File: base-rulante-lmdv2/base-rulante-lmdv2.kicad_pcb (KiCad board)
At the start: 2 copper layers, 94 x 78.7 mm, 27 parts, among them J1 RJ_can, J2 RJ_can, J3 connector_power, J4 connector_power, J5 connector_power, U1 Nucleo_STM32G431KB, U2 LMD18200, U3 LMD18200, U4 MCP2551-I-SN

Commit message: carte IO
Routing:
- net GND: vias 0 -> 1
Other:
- board text added: "12V"
- board text added: "Joel Imbergamo 2023-AAA"
- board text added: "USB"
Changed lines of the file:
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@@
     (fp_rect (start 14.351 -0.889) (end 16.129 36.449)
       (stroke (width 0.12) (type solid)) (fill none) (layer "F.SilkS"))
-    (fp_arc (start 3.967155 -10.260847) (mid 4.012946 -10.18528) (end 4.029561 -10.0985)
-      (stroke (width 0.12) (type solid)) (layer "F.SilkS"))
-    (fp_arc (start 4.151131 -10.424759) (mid 4.243716 -10.27088) (end 4.275977 -10.094215)
-      (stroke (width 0.12) (type solid)) (layer "F.SilkS"))
-    (fp_arc (start 4.625988 -10.535212) (mid 4.709184 -10.688639) (end 4.875989 -10.74)
+    (fp_arc (start 3.967155 -10.260847) (mid 4.012928 -10.185275) (end 4.029561 -10.0985)
+      (stroke (width 0.12) (type solid)) (layer "F.SilkS"))
+    (fp_arc (start 4.151131 -10.424759) (mid 4.243692 -10.270872) (end 4.275977 -10.094215)
+      (stroke (width 0.12) (type solid)) (layer "F.SilkS"))
+    (fp_arc (start 4.625988 -10.535212) (mid 4.709181 -10.688645) (end 4.875989 -10.74)
       (stroke (width 0.12) (type solid)) (layer "F.SilkS"))
     (fp_arc (start 4.625989 -10.391818) (mid 4.709183 -10.545247) (end 4.875989 -10.596605)
@@
     (fp_arc (start 4.625989 -10.189999) (mid 4.597956 -10.120573) (end 4.529578 -10.090064)
       (stroke (width 0.12) (type solid)) (layer "F.SilkS"))
-    (fp_arc (start 10.575989 -10.739999) (mid 10.742844 -10.688681) (end 10.825988 -10.535211)
-      (stroke (width 0.12) (type solid)) (layer "F.SilkS"))
-    (fp_arc (start 10.575989 -10.596605) (mid 10.742846 -10.545287) (end 10.825988 -10.391817)
+    (fp_arc (start 10.575989 -10.739999) (mid 10.742816 -10.688675) (end 10.825988 -10.535211)
+      (stroke (width 0.12) (type solid)) (layer "F.SilkS"))
+    (fp_arc (start 10.575989 -10.596605) (mid 10.742818 -10.545281) (end 10.825988 -10.391817)
       (stroke (width 0.12) (type solid)) (layer "F.SilkS"))
     (fp_arc (start 10.922399 -10.090063) (mid 10.854026 -10.120573) (end 10.825988 -10.19)
@@
   (gr_line (start 167.64 149.86) (end 114.3 149.86)
     (stroke (width 0.1) (type default)) (layer "Edge.Cuts"))
+  (gr_text "Joel Imbergamo\n2023-AAA" (at 83.82 147.32) (layer "F.Cu")
+    (effects (font (size 1.5 1.5) (thickness 0.3) bold) (justify left bottom))
+  )
+  (gr_text "12V" (at 137.16 144.78) (layer "F.Cu")
+    (effects (font (size 1.5 1.5) (thickness 0.3) bold) (justify left bottom))
+  )
+  (gr_text "USB" (at 114.3 73.66) (layer "F.Cu")
+    (effects (font (size 1.5 1.5) (thickness 0.3) bold) (justify left bottom))
+  )
   (segment (start 116.84 132.08) (end 116.84 134.62) (width 0.5) (layer "F.Cu") (net 1))
   (segment (start 114.3 99.06) (end 121.675539 91.684461) (width 0.25) (layer "F.Cu") (net 1))
@@
   (segment (start 88.1525 81.28) (end 86.36 81.28) (width 1) (layer "B.Cu") (net 1))
   (segment (start 81.28 86.36) (end 81.28 106.68) (width 1) (layer "B.Cu") (net 1))
+  (via (at 139.7 134.62) (size 0.8) (drill 0.4) (layers "F.Cu" "B.Cu") (free) (net 2))
   (segment (start 158.4925 98.24) (end 159.2 98.24) (width 1.8) (layer "F.Cu") (net 3))
   (segment (start 159.2 98.24) (end 160.02 99.06) (width 1.8) (layer "F.Cu") (net 3))

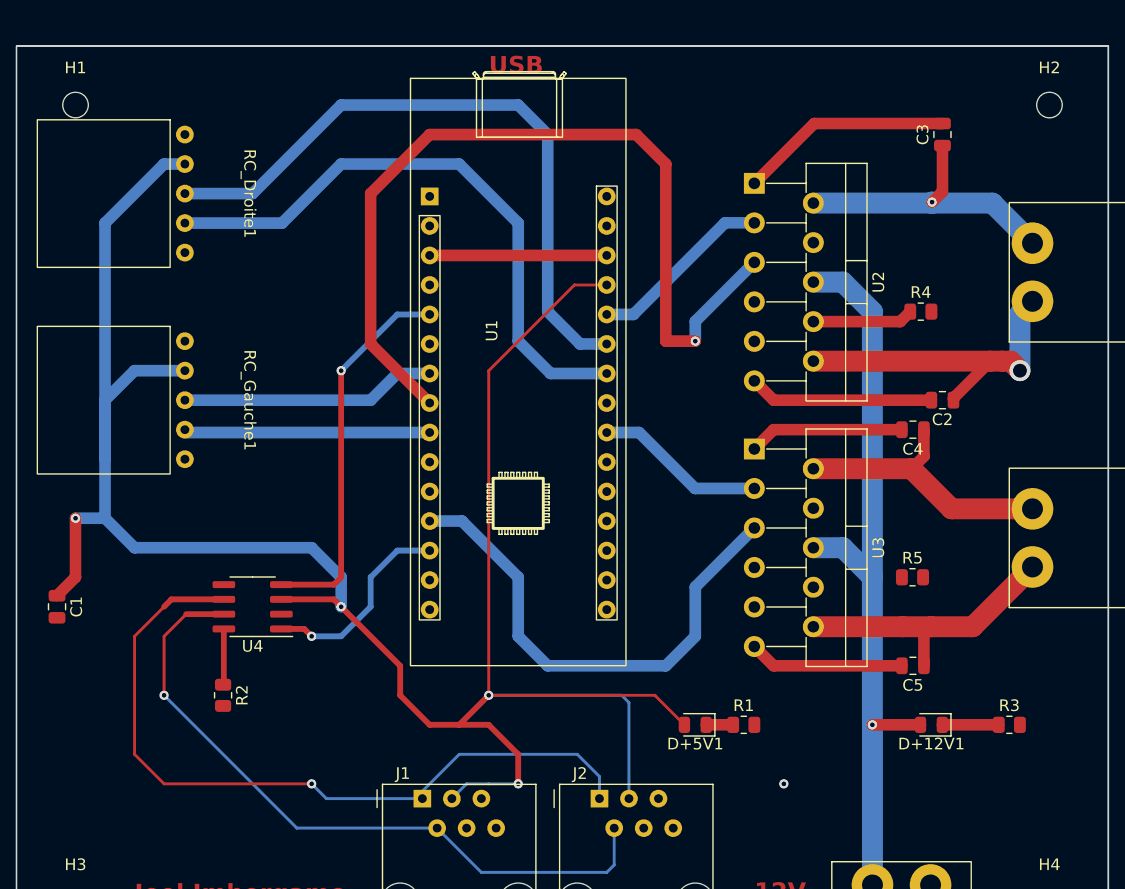
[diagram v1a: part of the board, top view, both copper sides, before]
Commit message: added some vias for the grownd plain
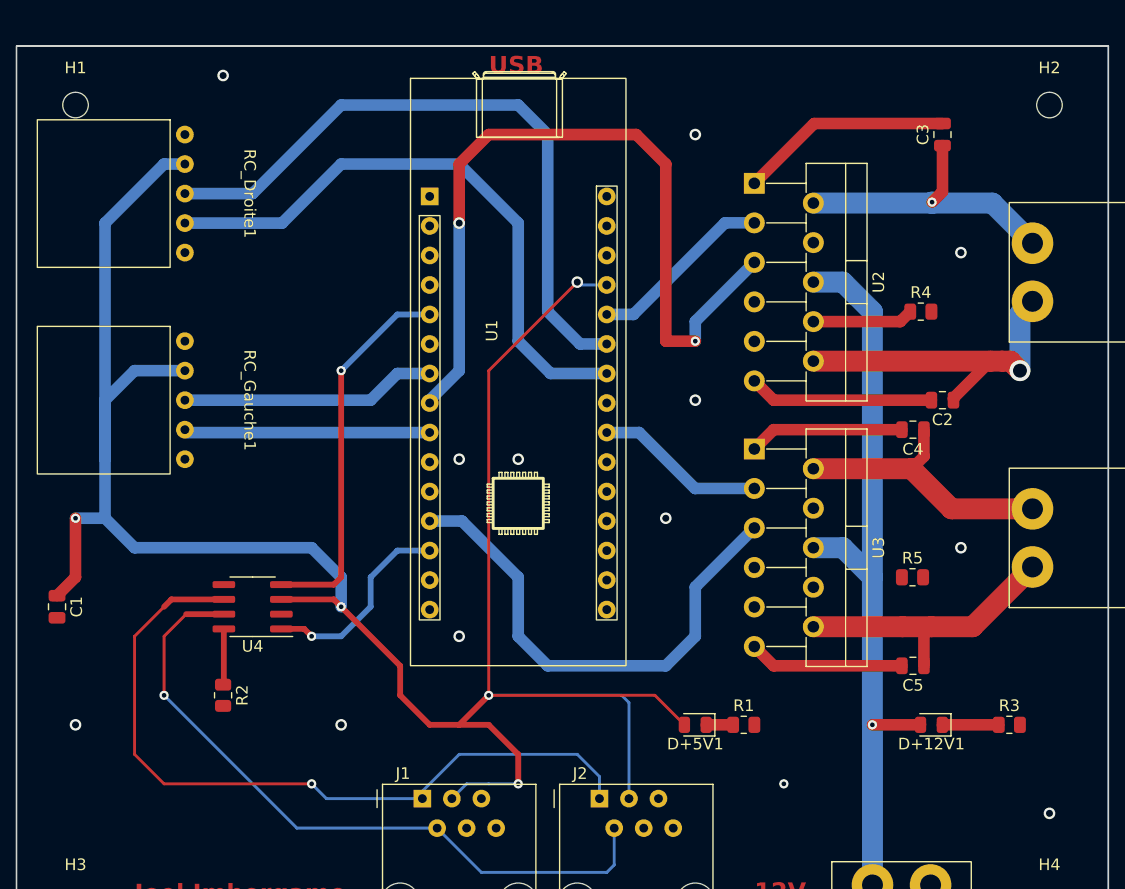
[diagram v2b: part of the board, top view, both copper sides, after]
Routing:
- net Net-(U1-~{RST}-Pad28): track 15.2 -> 0.00 mm
- net PWM_D: track 75.3 -> 68.2 mm, vias 1 -> 2
- net +5V: track 201.6 -> 202.2 mm, vias 4 -> 5
- net GND: vias 1 -> 13
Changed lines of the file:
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@@
     (pad_to_mask_clearance 0)
     (pcbplotparams
-      (layerselection 0x00010fc_ffffffff)
+      (layerselection 0x0001000_ffffffff)
       (plot_on_all_layers_selection 0x0000000_00000000)
       (disableapertmacros false)
@@
       (outputformat 1)
       (mirror false)
-      (drillshape 1)
+      (drillshape 0)
       (scaleselection 1)
-      (outputdirectory "")
+      (outputdirectory "../fab/")
     )
   )
@@
     (fp_rect (start 14.351 -0.889) (end 16.129 36.449)
       (stroke (width 0.12) (type solid)) (fill none) (layer "F.SilkS"))
-    (fp_arc (start 3.967155 -10.260847) (mid 4.012928 -10.185275) (end 4.029561 -10.0985)
-      (stroke (width 0.12) (type solid)) (layer "F.SilkS"))
-    (fp_arc (start 4.151131 -10.424759) (mid 4.243692 -10.270872) (end 4.275977 -10.094215)
-      (stroke (width 0.12) (type solid)) (layer "F.SilkS"))
-    (fp_arc (start 4.625988 -10.535212) (mid 4.709181 -10.688645) (end 4.875989 -10.74)
+    (fp_arc (start 3.967155 -10.260847) (mid 4.01291 -10.185271) (end 4.029561 -10.0985)
+      (stroke (width 0.12) (type solid)) (layer "F.SilkS"))
+    (fp_arc (start 4.151131 -10.424759) (mid 4.243705 -10.270873) (end 4.275977 -10.094215)
+      (stroke (width 0.12) (type solid)) (layer "F.SilkS"))
+    (fp_arc (start 4.625988 -10.535212) (mid 4.709181 -10.688641) (end 4.875989 -10.74)
       (stroke (width 0.12) (type solid)) (layer "F.SilkS"))
     (fp_arc (start 4.625989 -10.391818) (mid 4.709183 -10.545247) (end 4.875989 -10.596605)
@@
     (fp_arc (start 10.922399 -10.090063) (mid 10.854026 -10.120573) (end 10.825988 -10.19)
       (stroke (width 0.12) (type solid)) (layer "F.SilkS"))
-    (fp_arc (start 11.176 -10.094215) (mid 11.208256 -10.27088) (end 11.300846 -10.424759)
-      (stroke (width 0.12) (type solid)) (layer "F.SilkS"))
-    (fp_arc (start 11.422416 -10.0985) (mid 11.439038 -10.18528) (end 11.484822 -10.260847)
+    (fp_arc (start 11.176 -10.094215) (mid 11.208251 -10.270884) (end 11.300846 -10.424759)
+      (stroke (width 0.12) (type solid)) (layer "F.SilkS"))
+    (fp_arc (start 11.422416 -10.0985) (mid 11.439043 -10.185276) (end 11.484822 -10.260847)
       (stroke (width 0.12) (type solid)) (layer "F.SilkS"))
     (fp_circle (center 5.969 28.067) (end 5.969001 28.067)
@@
   )
   (segment (start 116.84 132.08) (end 116.84 134.62) (width 0.5) (layer "F.Cu") (net 1))
-  (segment (start 114.3 99.06) (end 121.675539 91.684461) (width 0.25) (layer "F.Cu") (net 1))
+  (segment (start 114.3 99.06) (end 121.92 91.44) (width 0.25) (layer "F.Cu") (net 1))
   (segment (start 101.6 119.38) (end 106.68 124.46) (width 0.5) (layer "F.Cu") (net 1))
   (segment (start 128.6025 127) (end 114.3 127) (width 0.25) (layer "F.Cu") (net 1))
@@
   (segment (start 106.68 124.46) (end 106.68 127) (width 0.5) (layer "F.Cu") (net 1))
   (segment (start 96.455 118.745) (end 100.965 118.745) (width 0.5) (layer "F.Cu") (net 1))
-  (segment (start 121.675539 91.684461) (end 124.46 91.684461) (width 0.25) (layer "F.Cu") (net 1))
   (segment (start 100.965 118.745) (end 101.6 119.38) (width 0.5) (layer "F.Cu") (net 1))
   (segment (start 111.76 129.54) (end 114.3 127) (width 0.5) (layer "F.Cu") (net 1))
+  (segment (start 121.92 91.44) (end 121.675539 91.684461) (width 0.25) (layer "F.Cu") (net 1))
   (segment (start 114.3 127) (end 114.3 99.06) (width 0.25) (layer "F.Cu") (net 1))
   (segment (start 111.76 129.54) (end 114.3 129.54) (width 0.5) (layer "F.Cu") (net 1))
@@
   (via (at 116.84 134.62) (size 0.8) (drill 0.4) (layers "F.Cu" "B.Cu") (net 1))
   (via (at 78.74 111.76) (size 0.8) (drill 0.4) (layers "F.Cu" "B.Cu") (net 1))
+  (via (at 121.92 91.44) (size 1) (drill 0.6) (layers "F.Cu" "B.Cu") (net 1))
   (via (at 114.3 127) (size 0.8) (drill 0.4) (layers "F.Cu" "B.Cu") (net 1))
   (segment (start 88.1525 99.06) (end 83.82 99.06) (width 1) (layer "B.Cu") (net 1))
   (segment (start 126.37 135.89) (end 126.37 127.63) (width 0.25) (layer "B.Cu") (net 1))
+  (segment (start 122.164461 91.684461) (end 124.46 91.684461) (width 0.25) (layer "B.Cu") (net 1))
   (segment (start 86.36 81.28) (end 81.28 86.36) (width 1) (layer "B.Cu") (net 1))
   (segment (start 126.37 127.63) (end 125.74 127) (width 0.25) (layer "B.Cu") (net 1))
@@
   (segment (start 83.82 99.06) (end 81.28 101.6) (width 1) (layer "B.Cu") (net 1))
   (segment (start 111.13 135.89) (end 112.4 134.62) (width 0.25) (layer "B.Cu") (net 1))
+  (segment (start 121.92 91.44) (end 122.164461 91.684461) (width 0.25) (layer "B.Cu") (net 1))
   (segment (start 81.28 111.76) (end 83.82 114.3) (width 1) (layer "B.Cu") (net 1))
   (segment (start 99.06 114.3) (end 101.6 116.84) (width 1) (layer "B.Cu") (net 1))
@@
   (segment (start 88.1525 81.28) (end 86.36 81.28) (width 1) (layer "B.Cu") (net 1))
   (segment (start 81.28 86.36) (end 81.28 106.68) (width 1) (layer "B.Cu") (net 1))
+  (via (at 101.6 129.54) (size 1) (drill 0.6) (layers "F.Cu" "B.Cu") (free) (net 2))
+  (via (at 154.94 114.3) (size 1) (drill 0.6) (layers "F.Cu" "B.Cu") (free) (net 2))
+  (via (at 111.76 121.92) (size 1) (drill 0.6) (layers "F.Cu" "B.Cu") (free) (net 2))
   (via (at 139.7 134.62) (size 0.8) (drill 0.4) (layers "F.Cu" "B.Cu") (free) (net 2))
+  (via (at 132.08 78.74) (size 1) (drill 0.6) (layers "F.Cu" "B.Cu") (free) (net 2))
+  (via (at 132.08 101.6) (size 1) (drill 0.6) (layers "F.Cu" "B.Cu") (free) (net 2))
+  (via (at 162.56 137.16) (size 1) (drill 0.6) (layers "F.Cu" "B.Cu") (free) (net 2))
+  (via (at 78.74 129.54) (size 1) (drill 0.6) (layers "F.Cu" "B.Cu") (free) (net 2))
+  (via (at 154.94 88.9) (size 1) (drill 0.6) (layers "F.Cu" "B.Cu") (free) (net 2))
+  (via (at 116.84 106.68) (size 1) (drill 0.6) (layers "F.Cu" "B.Cu") (free) (net 2))
+  (via (at 111.76 106.68) (size 1) (drill 0.6) (layers "F.Cu" "B.Cu") (free) (net 2))
+  (via (at 129.54 111.76) (size 1) (drill 0.6) (layers "F.Cu" "B.Cu") (free) (net 2))
+  (via (at 91.44 73.66) (size 1) (drill 0.6) (layers "F.Cu" "B.Cu") (free) (net 2))
   (segment (start 158.4925 98.24) (end 159.2 98.24) (width 1.8) (layer "F.Cu") (net 3))
   (segment (start 159.2 98.24) (end 160.02 99.06) (width 1.8) (layer "F.Cu") (net 3))
@@
   (segment (start 109.22 104.384461) (end 88.396961 104.384461) (width 1) (layer "B.Cu") (net 27))
   (segment (start 88.396961 104.384461) (end 88.1525 104.14) (width 1) (layer "B.Cu") (net 27))
-  (segment (start 109.22 89.144461) (end 124.46 89.144461) (width 1) (layer "F.Cu") (net 31))
   (segment (start 96.455 117.475) (end 100.965 117.475) (width 0.5) (layer "F.Cu") (net 32))
   (segment (start 101.6 116.84) (end 101.6 99.06) (width 0.5) (layer "F.Cu") (net 32))
@@
   (segment (start 106.435539 94.224461) (end 109.22 94.224461) (width 0.5) (layer "B.Cu") (net 32))
   (segment (start 101.6 99.06) (end 106.435539 94.224461) (width 0.5) (layer "B.Cu") (net 32))
-  (segment (start 104.14 96.764461) (end 109.22 101.844461) (width 1) (layer "F.Cu") (net 34))
   (segment (start 129.54 81.28) (end 127 78.74) (width 1) (layer "F.Cu") (net 34))
-  (segment (start 109.22 78.74) (end 104.14 83.82) (width 1) (layer "F.Cu") (net 34))
+  (segment (start 111.76 86.36) (end 111.76 81.28) (width 1) (layer "F.Cu") (net 34))
   (segment (start 132.08 96.52) (end 129.54 96.52) (width 1) (layer "F.Cu") (net 34))
+  (segment (start 127 78.74) (end 114.3 78.74) (width 1) (layer "F.Cu") (net 34))
   (segment (start 129.54 96.52) (end 129.54 81.28) (width 1) (layer "F.Cu") (net 34))
-  (segment (start 104.14 83.82) (end 104.14 96.764461) (width 1) (layer "F.Cu") (net 34))
-  (segment (start 127 78.74) (end 109.22 78.74) (width 1) (layer "F.Cu") (net 34))
+  (segment (start 111.76 81.28) (end 114.3 78.74) (width 1) (layer "F.Cu") (net 34))
+  (via (at 111.76 86.36) (size 1) (drill 0.6) (layers "F.Cu" "B.Cu") (net 34))
   (via (at 132.08 96.52) (size 0.8) (drill 0.4) (layers "F.Cu" "B.Cu") (net 34))
+  (segment (start 109.22 101.844461) (end 109.22 101.6) (width 1) (layer "B.Cu") (net 34))
   (segment (start 137.16 89.74) (end 132.08 94.82) (width 1) (layer "B.Cu") (net 34))
+  (segment (start 111.76 99.06) (end 111.76 86.36) (width 1) (layer "B.Cu") (net 34))
+  (segment (start 109.22 101.6) (end 111.76 99.06) (width 1) (layer "B.Cu") (net 34))
   (segment (start 132.08 94.82) (end 132.08 96.52) (width 1) (layer "B.Cu") (net 34))
   (segment (start 137.16 112.6) (end 132.08 117.68) (width 1) (layer "B.Cu") (net 37))
